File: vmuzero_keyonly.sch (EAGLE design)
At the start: 10 parts

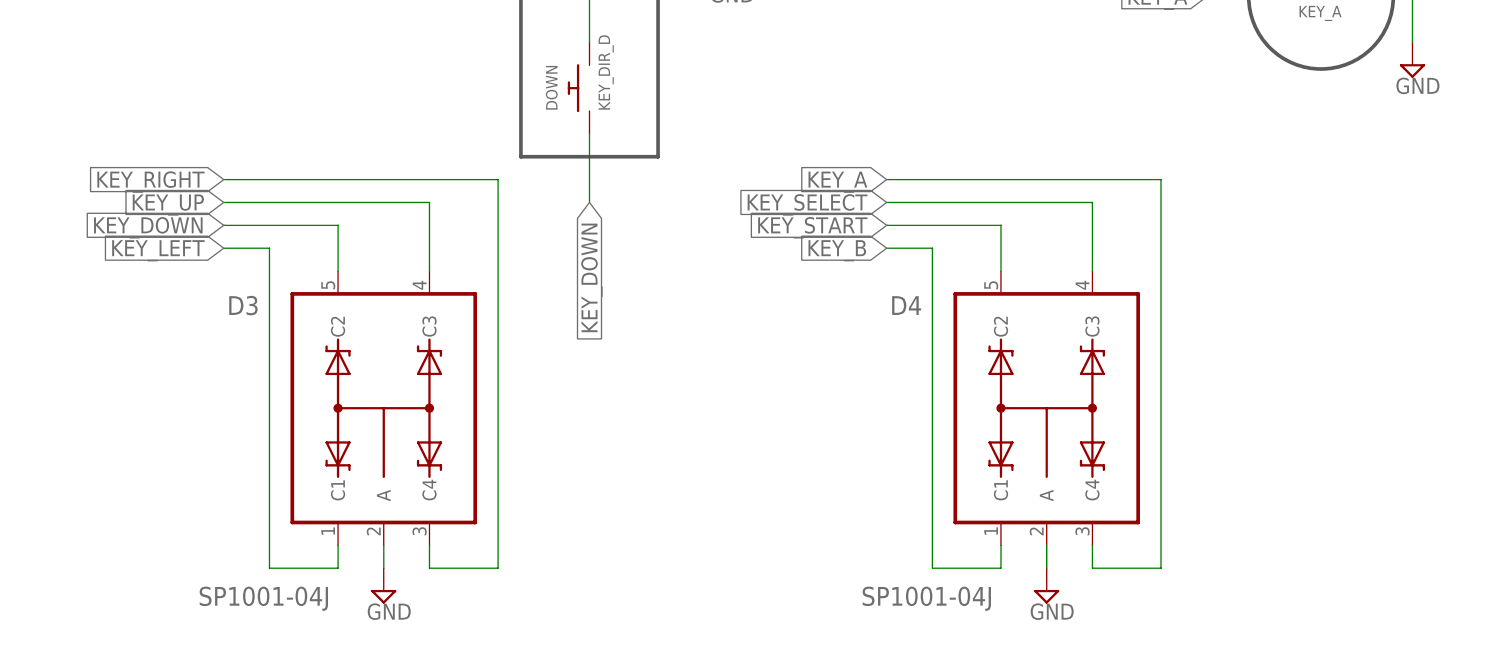
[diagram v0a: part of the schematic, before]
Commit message: Changed height to 24.5
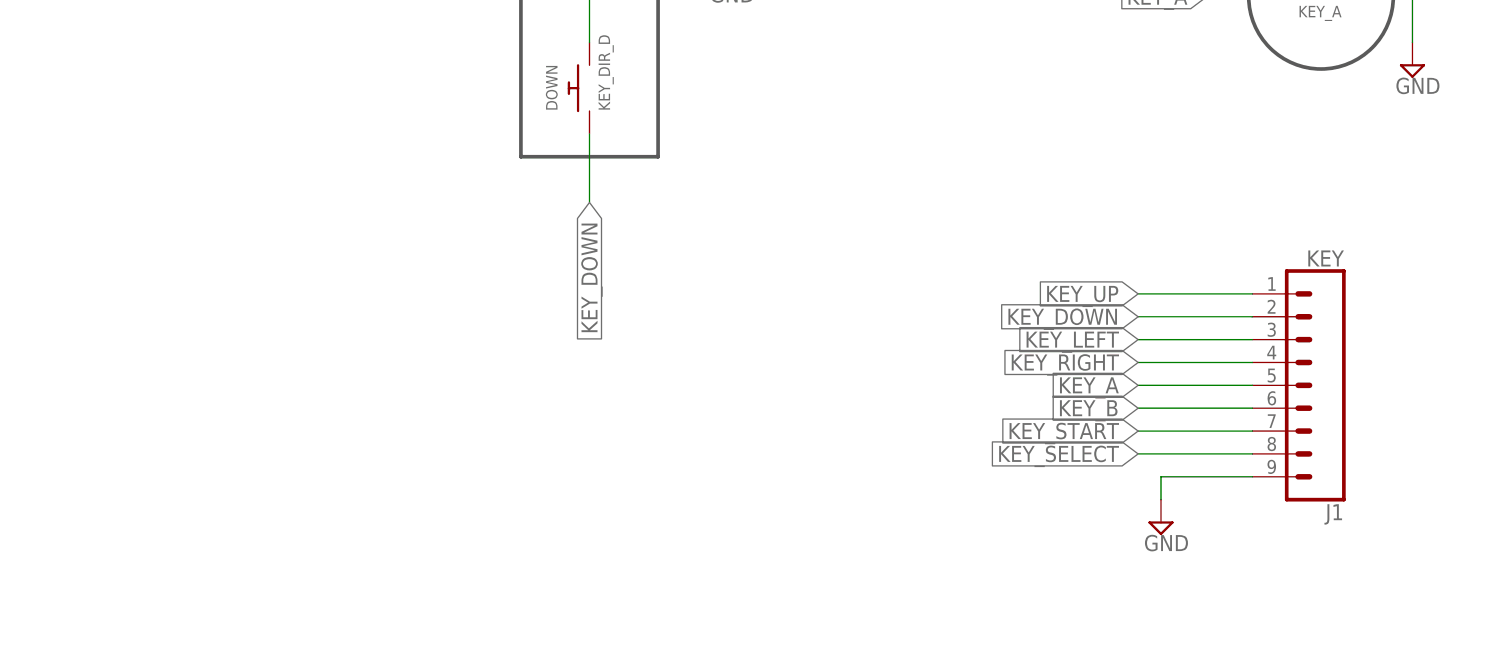
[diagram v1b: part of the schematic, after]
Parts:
- removed D3, D4: SP1001-04J, vmuzero:SP1001-04J
- added J1: KEY, SparkFun-Connectors:CONN_09NO_SILK
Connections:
- net GND: now also J1.9; no longer D3.A, D4.A
- net KEY_A: now also J1.5; no longer D4.C4
- net KEY_B: now also J1.6; no longer D4.C1
- net KEY_DOWN: now also J1.2; no longer D3.C2
- net KEY_LEFT: now also J1.3; no longer D3.C1
- net KEY_RIGHT: now also J1.4; no longer D3.C4
- net KEY_SELECT: now also J1.8; no longer D4.C3
- net KEY_START: now also J1.7; no longer D4.C2
- net KEY_UP: now also J1.1; no longer D3.C3
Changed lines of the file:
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@@
 <part name="SUPPLY38" library="supply2" deviceset="GND" device=""/>
 <part name="SUPPLY39" library="supply2" deviceset="GND" device=""/>
-<part name="D3" library="vmuzero" deviceset="SP1001-04" device="J"/>
-<part name="SUPPLY53" library="supply2" deviceset="GND" device=""/>
-<part name="D4" library="vmuzero" deviceset="SP1001-04" device="J"/>
 <part name="SUPPLY54" library="supply2" deviceset="GND" device=""/>
+<part name="J1" library="SparkFun-Connectors" deviceset="CONN_09" device="NO_SILK" value="KEY"/>
 </parts>
 <sheets>
@@
 <instance part="SUPPLY38" gate="GND" x="157.48" y="114.3"/>
 <instance part="SUPPLY39" gate="GND" x="86.36" y="81.28"/>
-<instance part="D3" gate="G$1" x="48.26" y="33.02" smashed="yes">
-<attribute name="NAME" x="30.8356" y="43.3832" size="2.0828" layer="95" ratio="10" rot="SR0"/>
-<attribute name="VALUE" x="27.6352" y="11.0744" size="2.0828" layer="96" ratio="10" rot="SR0"/>
-</instance>
-<instance part="SUPPLY53" gate="GND" x="48.26" y="12.7"/>
-<instance part="D4" gate="G$1" x="121.92" y="33.02" smashed="yes">
-<attribute name="NAME" x="104.4956" y="43.3832" size="2.0828" layer="95" ratio="10" rot="SR0"/>
-<attribute name="VALUE" x="101.2952" y="11.0744" size="2.0828" layer="96" ratio="10" rot="SR0"/>
-</instance>
-<instance part="SUPPLY54" gate="GND" x="121.92" y="12.7"/>
+<instance part="SUPPLY54" gate="GND" x="134.62" y="20.32"/>
+<instance part="J1" gate="G$1" x="154.94" y="35.56" rot="R180"/>
 </instances>
 <busses>
@@
 </segment>
 <segment>
-<pinref part="D3" gate="G$1" pin="A"/>
-<pinref part="SUPPLY53" gate="GND" pin="GND"/>
-<wire x1="48.26" y1="15.24" x2="48.26" y2="17.78" width="0.1524" layer="91"/>
-</segment>
-<segment>
-<pinref part="D4" gate="G$1" pin="A"/>
 <pinref part="SUPPLY54" gate="GND" pin="GND"/>
-<wire x1="121.92" y1="15.24" x2="121.92" y2="17.78" width="0.1524" layer="91"/>
+<wire x1="134.62" y1="22.86" x2="134.62" y2="25.4" width="0.1524" layer="91"/>
+<pinref part="J1" gate="G$1" pin="9"/>
+<wire x1="144.78" y1="25.4" x2="134.62" y2="25.4" width="0.1524" layer="91"/>
 </segment>
 </net>
@@
 </segment>
 <segment>
-<wire x1="104.14" y1="50.8" x2="109.22" y2="50.8" width="0.1524" layer="91"/>
-<wire x1="109.22" y1="50.8" x2="109.22" y2="15.24" width="0.1524" layer="91"/>
-<wire x1="109.22" y1="15.24" x2="116.84" y2="15.24" width="0.1524" layer="91"/>
-<pinref part="D4" gate="G$1" pin="C1"/>
-<wire x1="116.84" y1="15.24" x2="116.84" y2="17.78" width="0.1524" layer="91"/>
-<label x="104.14" y="50.8" size="1.778" layer="95" rot="R180" xref="yes"/>
+<wire x1="132.08" y1="33.02" x2="144.78" y2="33.02" width="0.1524" layer="91"/>
+<label x="132.08" y="33.02" size="1.778" layer="95" rot="R180" xref="yes"/>
+<pinref part="J1" gate="G$1" pin="6"/>
 </segment>
 </net>
@@
 </segment>
 <segment>
-<wire x1="104.14" y1="58.42" x2="134.62" y2="58.42" width="0.1524" layer="91"/>
-<wire x1="134.62" y1="58.42" x2="134.62" y2="15.24" width="0.1524" layer="91"/>
-<wire x1="134.62" y1="15.24" x2="127" y2="15.24" width="0.1524" layer="91"/>
-<pinref part="D4" gate="G$1" pin="C4"/>
-<wire x1="127" y1="15.24" x2="127" y2="17.78" width="0.1524" layer="91"/>
-<label x="104.14" y="58.42" size="1.778" layer="95" rot="R180" xref="yes"/>
+<wire x1="132.08" y1="35.56" x2="144.78" y2="35.56" width="0.1524" layer="91"/>
+<label x="132.08" y="35.56" size="1.778" layer="95" rot="R180" xref="yes"/>
+<pinref part="J1" gate="G$1" pin="5"/>
 </segment>
 </net>
@@
 </segment>
 <segment>
-<wire x1="104.14" y1="53.34" x2="116.84" y2="53.34" width="0.1524" layer="91"/>
-<pinref part="D4" gate="G$1" pin="C2"/>
-<wire x1="116.84" y1="53.34" x2="116.84" y2="48.26" width="0.1524" layer="91"/>
-<label x="104.14" y="53.34" size="1.778" layer="95" rot="R180" xref="yes"/>
+<wire x1="132.08" y1="30.48" x2="144.78" y2="30.48" width="0.1524" layer="91"/>
+<label x="132.08" y="30.48" size="1.778" layer="95" rot="R180" xref="yes"/>
+<pinref part="J1" gate="G$1" pin="7"/>
 </segment>
 </net>
@@
 </segment>
 <segment>
-<wire x1="104.14" y1="55.88" x2="127" y2="55.88" width="0.1524" layer="91"/>
-<pinref part="D4" gate="G$1" pin="C3"/>
-<wire x1="127" y1="55.88" x2="127" y2="48.26" width="0.1524" layer="91"/>
-<label x="104.14" y="55.88" size="1.778" layer="95" rot="R180" xref="yes"/>
+<wire x1="132.08" y1="27.94" x2="144.78" y2="27.94" width="0.1524" layer="91"/>
+<label x="132.08" y="27.94" size="1.778" layer="95" rot="R180" xref="yes"/>
+<pinref part="J1" gate="G$1" pin="8"/>
 </segment>
 </net>
@@
 </segment>
 <segment>
-<wire x1="30.48" y1="50.8" x2="35.56" y2="50.8" width="0.1524" layer="91"/>
-<wire x1="35.56" y1="50.8" x2="35.56" y2="15.24" width="0.1524" layer="91"/>
-<wire x1="35.56" y1="15.24" x2="43.18" y2="15.24" width="0.1524" layer="91"/>
-<pinref part="D3" gate="G$1" pin="C1"/>
-<wire x1="43.18" y1="15.24" x2="43.18" y2="17.78" width="0.1524" layer="91"/>
-<label x="30.48" y="50.8" size="1.778" layer="95" rot="R180" xref="yes"/>
+<wire x1="132.08" y1="40.64" x2="144.78" y2="40.64" width="0.1524" layer="91"/>
+<label x="132.08" y="40.64" size="1.778" layer="95" rot="R180" xref="yes"/>
+<pinref part="J1" gate="G$1" pin="3"/>
 </segment>
 </net>
@@
 </segment>
 <segment>
-<wire x1="30.48" y1="55.88" x2="53.34" y2="55.88" width="0.1524" layer="91"/>
-<pinref part="D3" gate="G$1" pin="C3"/>
-<wire x1="53.34" y1="55.88" x2="53.34" y2="48.26" width="0.1524" layer="91"/>
-<label x="30.48" y="55.88" size="1.778" layer="95" rot="R180" xref="yes"/>
+<wire x1="132.08" y1="45.72" x2="144.78" y2="45.72" width="0.1524" layer="91"/>
+<label x="132.08" y="45.72" size="1.778" layer="95" rot="R180" xref="yes"/>
+<pinref part="J1" gate="G$1" pin="1"/>
 </segment>
 </net>
@@
 </segment>
 <segment>
-<wire x1="30.48" y1="58.42" x2="60.96" y2="58.42" width="0.1524" layer="91"/>
-<wire x1="60.96" y1="58.42" x2="60.96" y2="15.24" width="0.1524" layer="91"/>
-<wire x1="60.96" y1="15.24" x2="53.34" y2="15.24" width="0.1524" layer="91"/>
-<pinref part="D3" gate="G$1" pin="C4"/>
-<wire x1="53.34" y1="15.24" x2="53.34" y2="17.78" width="0.1524" layer="91"/>
-<label x="30.48" y="58.42" size="1.778" layer="95" rot="R180" xref="yes"/>
+<wire x1="132.08" y1="38.1" x2="144.78" y2="38.1" width="0.1524" layer="91"/>
+<label x="132.08" y="38.1" size="1.778" layer="95" rot="R180" xref="yes"/>
+<pinref part="J1" gate="G$1" pin="4"/>
 </segment>
 </net>
@@
 </segment>
 <segment>
-<wire x1="30.48" y1="53.34" x2="43.18" y2="53.34" width="0.1524" layer="91"/>
-<pinref part="D3" gate="G$1" pin="C2"/>
-<wire x1="43.18" y1="53.34" x2="43.18" y2="48.26" width="0.1524" layer="91"/>
-<label x="30.48" y="53.34" size="1.778" layer="95" rot="R180" xref="yes"/>
+<wire x1="132.08" y1="43.18" x2="144.78" y2="43.18" width="0.1524" layer="91"/>
+<label x="132.08" y="43.18" size="1.778" layer="95" rot="R180" xref="yes"/>
+<pinref part="J1" gate="G$1" pin="2"/>
 </segment>
 </net>
